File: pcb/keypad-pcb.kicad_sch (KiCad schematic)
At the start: 16 parts, among them SW1 SW_Push, U1 ATmega32U4-A, Y1 Crystal_GND24_Small

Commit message: schematic complete
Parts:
- added D1, D2: D_Small, symbol Device:D_Small
- added MX1, MX2: MX-NoLED, symbol MX_Alps_Hybrid:MX-NoLED
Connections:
- new net: D1.2 (A), MX1.2 (ROW)
- new net: D2.2 (A), MX2.2 (ROW)
- new net COL0: MX1.1 (COL)
- new net COL1: MX2.1 (COL)
- new net ROW0: D1.1 (K), D2.1 (K)

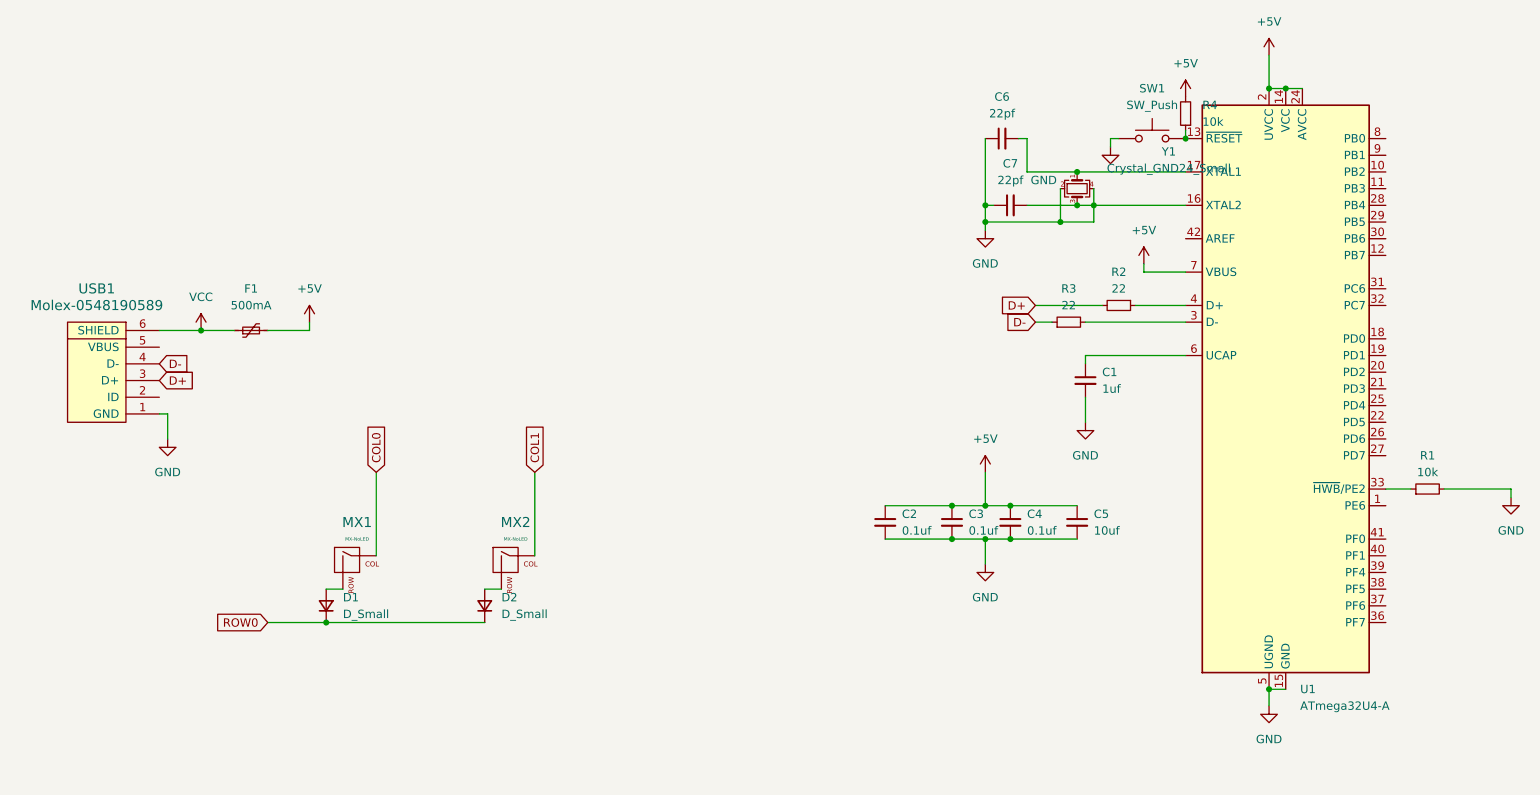
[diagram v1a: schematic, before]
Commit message: reorganized schematic and added footprints
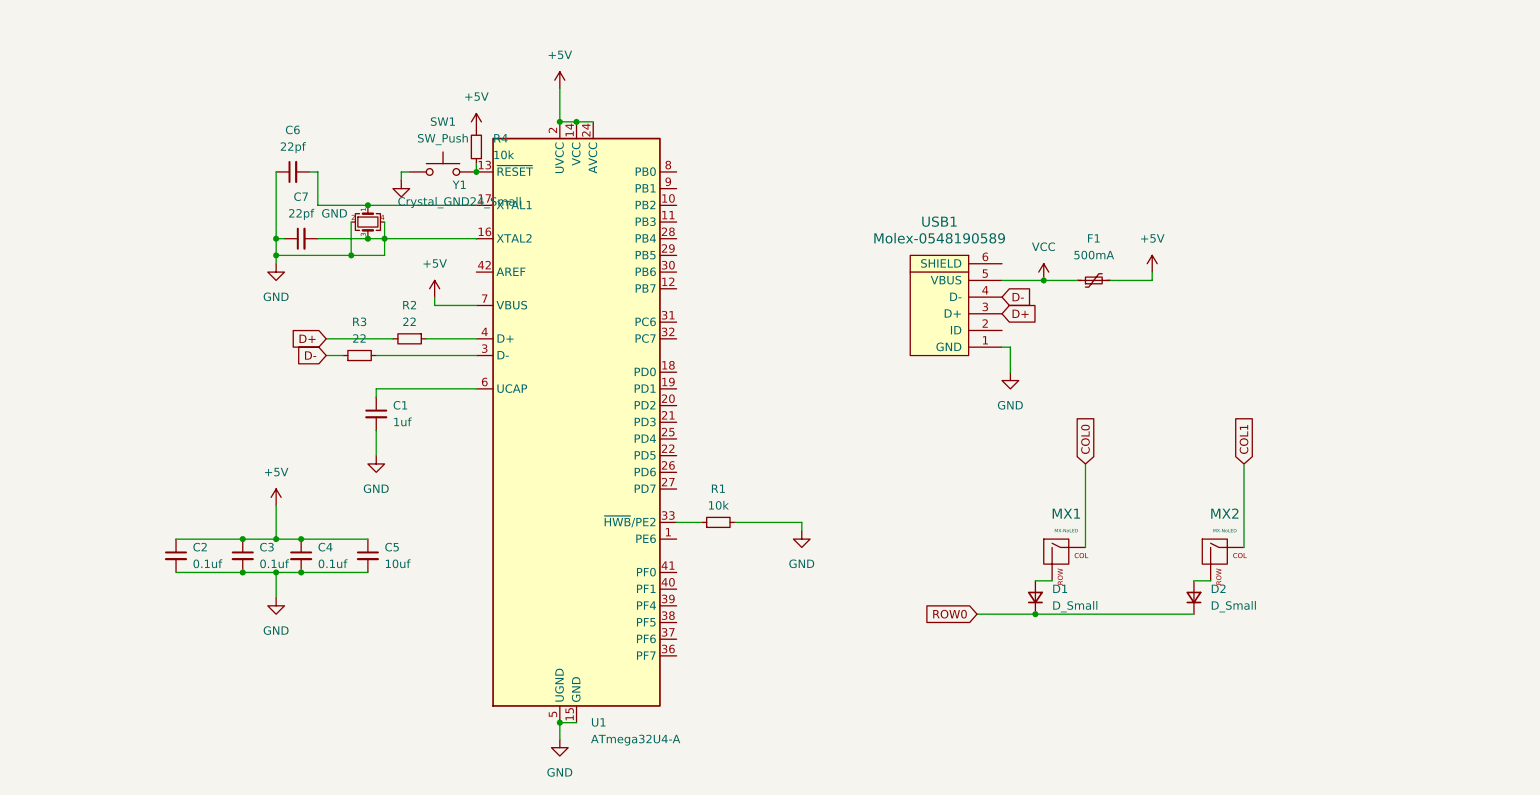
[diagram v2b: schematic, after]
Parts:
- C1, C2, C3, C4, C5, C6, C7: footprint (none) -> Capacitor_SMD:C_0805_2012Metric
- D1, D2: footprint (none) -> Diode_SMD:D_SOD-123
- F1: footprint (none) -> Fuse:Fuse_1206_3216Metric
- MX1, MX2: footprint (none) -> MX_Alps_Hybrid:MX-1U-NoLED
- R1, R2, R3, R4: footprint (none) -> Resistor_SMD:R_0805_2012Metric
- SW1: footprint (none) -> random-keyboard-parts:SKQG-1155865
- USB1: footprint (none) -> random-keyboard-parts:Molex-0548190589
- Y1: footprint (none) -> Crystal:Crystal_SMD_3225-4Pin_3.2x2.5mm
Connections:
- net VCC: now also USB1.5 (VBUS); no longer USB1.6 (SHIELD)
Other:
- moved on the sheet: C1, C2, C3, C4, C5, C6, C7, D1, D2, F1, MX1, MX2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

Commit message: pcb layout done
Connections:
- net COL0: now also U1.27 (PD7)
- net COL1: now also U1.29 (PB5)
- net GND: no longer C7.2, U1.16 (XTAL2), Y1.3
- net ROW0: now also U1.28 (PB4)
- new net: C7.2, U1.16 (XTAL2), Y1.3
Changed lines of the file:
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@@
 	(paper "A4")
 	(junction
-		(at 73.66 55.88)
-		(diameter 0)
-		(color 0 0 0 0)
-	)
-	(junction
 		(at 60.96 101.6)
 		(diameter 0)
@@
 	(wire
 		(pts
-			(xy 71.12 55.88) (xy 73.66 55.88)
-		)
-		(stroke
-			(width 0)
-			(type default)
-		)
-	)
-	(wire
-		(pts
 			(xy 100.33 38.1) (xy 102.87 38.1)
 		)
@@
 	(wire
 		(pts
-			(xy 73.66 55.88) (xy 73.66 58.42)
-		)
-		(stroke
-			(width 0)
-			(type default)
-		)
-	)
-	(wire
-		(pts
 			(xy 87.63 66.04) (xy 81.28 66.04)
 		)
@@
 	(wire
 		(pts
-			(xy 73.66 53.34) (xy 73.66 55.88)
+			(xy 73.66 53.34) (xy 73.66 58.42)
 		)
 		(stroke
@@
 	(wire
 		(pts
-			(xy 73.66 55.88) (xy 87.63 55.88)
+			(xy 71.12 55.88) (xy 87.63 55.88)
 		)
 		(stroke
@@
 			(effects
 				(font
+					(size 1.27 1.27)
+				)
+				(justify left)
+				(hide yes)
+			)
+		)
+	)
+	(global_label "ROW0"
+		(shape input)
+		(at 118.11 55.88 0)
+		(fields_autoplaced yes)
+		(effects
+			(font
+				(size 1.27 1.27)
+			)
+			(justify left)
+		)
+		(property "Intersheetrefs" "${INTERSHEET_REFS}"
+			(at 126.3566 55.88 0)
+			(effects
+				(font
+					(size 1.27 1.27)
+				)
+				(justify left)
+				(hide yes)
+			)
+		)
+	)
+	(global_label "COL0"
+		(shape input)
+		(at 118.11 93.98 0)
+		(fields_autoplaced yes)
+		(effects
+			(font
+				(size 1.27 1.27)
+			)
+			(justify left)
+		)
+		(property "Intersheetrefs" "${INTERSHEET_REFS}"
+			(at 125.9333 93.98 0)
+			(effects
+				(font
+					(size 1.27 1.27)
+				)
+				(justify left)
+				(hide yes)
+			)
+		)
+	)
+	(global_label "COL1"
+		(shape input)
+		(at 118.11 58.42 0)
+		(fields_autoplaced yes)
+		(effects
+			(font
+				(size 1.27 1.27)
+			)
+			(justify left)
+		)
+		(property "Intersheetrefs" "${INTERSHEET_REFS}"
+			(at 125.9333 58.42 0)
+			(effects
+				(font

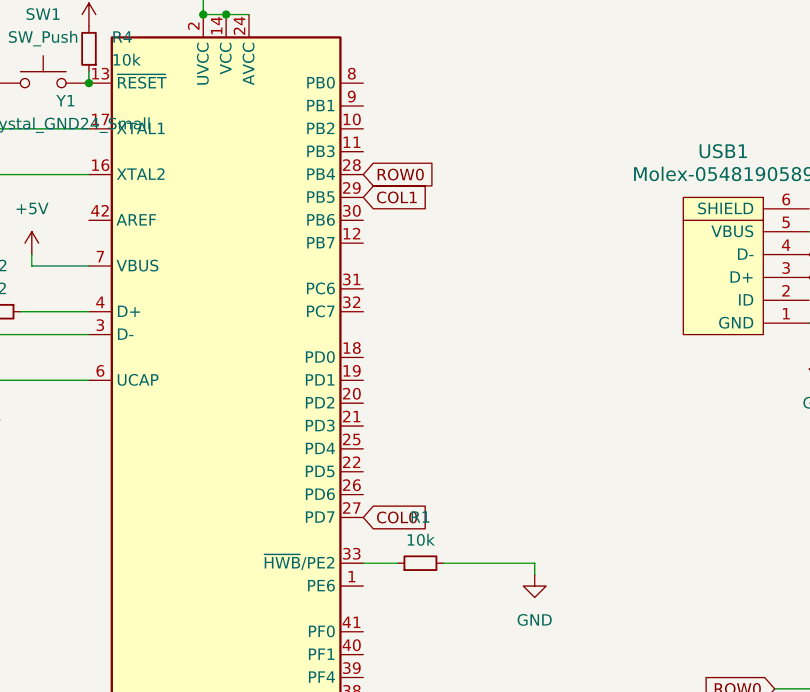
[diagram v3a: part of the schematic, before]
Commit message: redesigned pcb for front-facing usb
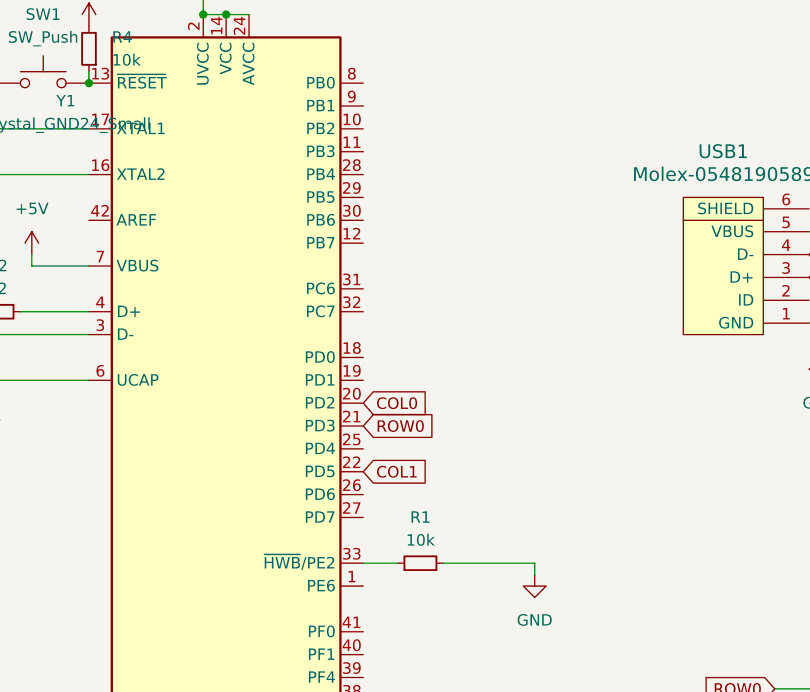
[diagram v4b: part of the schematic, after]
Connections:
- net COL0: now also U1.20 (PD2); no longer U1.27 (PD7)
- net COL1: now also U1.22 (PD5); no longer U1.29 (PB5)
- net ROW0: now also U1.21 (PD3); no longer U1.28 (PB4)
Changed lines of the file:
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@@
 	(global_label "ROW0"
 		(shape input)
-		(at 118.11 55.88 0)
+		(at 118.11 83.82 0)
 		(fields_autoplaced yes)
 		(effects
@@
 		)
 		(property "Intersheetrefs" "${INTERSHEET_REFS}"
-			(at 126.3566 55.88 0)
+			(at 126.3566 83.82 0)
 			(effects
 				(font
@@
 	(global_label "COL0"
 		(shape input)
-		(at 118.11 93.98 0)
+		(at 118.11 81.28 0)
 		(fields_autoplaced yes)
 		(effects
@@
 		)
 		(property "Intersheetrefs" "${INTERSHEET_REFS}"
-			(at 125.9333 93.98 0)
+			(at 125.9333 81.28 0)
 			(effects
 				(font
@@
 	(global_label "COL1"
 		(shape input)
-		(at 118.11 58.42 0)
+		(at 118.11 88.9 0)
 		(fields_autoplaced yes)
 		(effects
@@
 		)
 		(property "Intersheetrefs" "${INTERSHEET_REFS}"
-			(at 125.9333 58.42 0)
+			(at 125.9333 88.9 0)
 			(effects
 				(font
